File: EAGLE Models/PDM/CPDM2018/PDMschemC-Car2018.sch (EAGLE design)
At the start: 26 parts

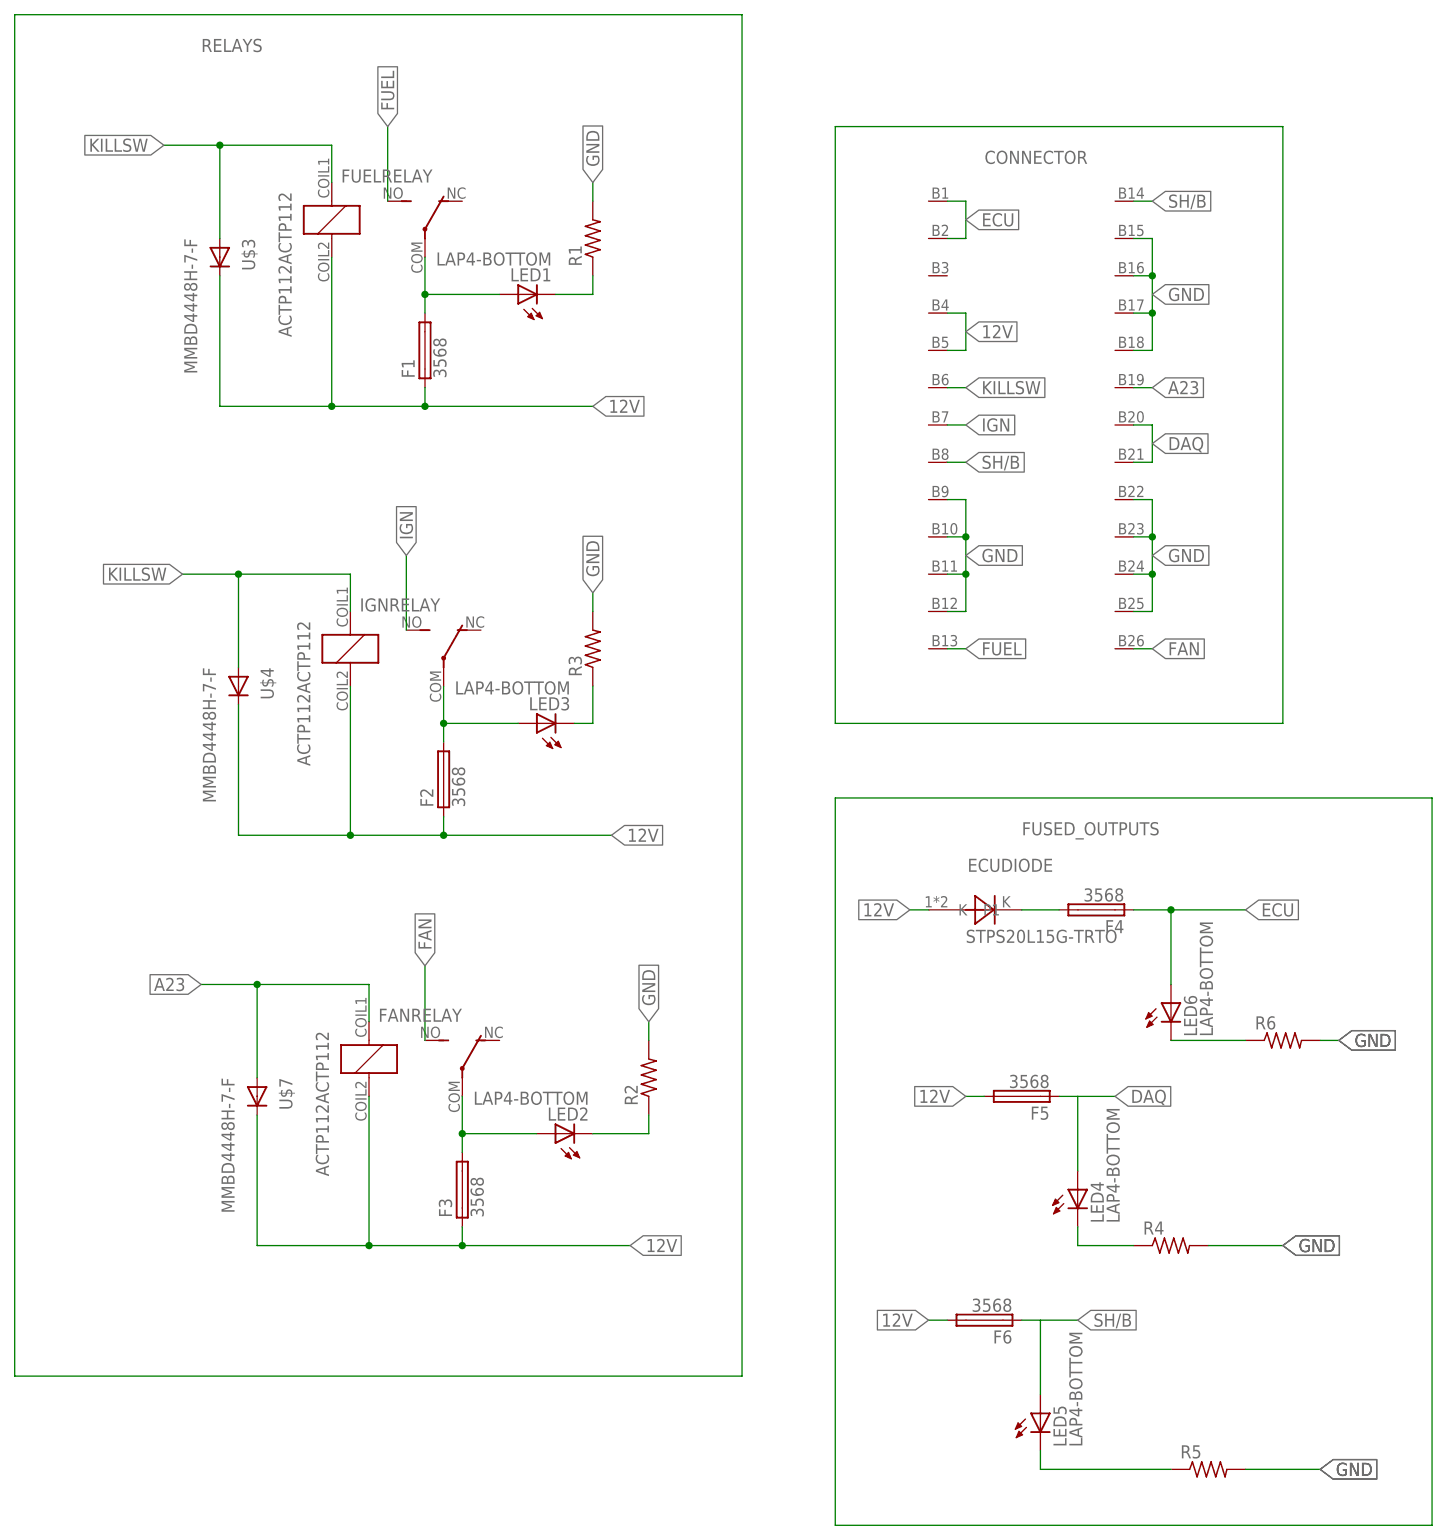
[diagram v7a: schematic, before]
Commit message: Made changes to PDM board
replaced LEDs and Resistors with correct device/package
made ground plane on both layers
named all planes to remove airwires
added resistor values to schem
connected ignition trace to ign relay
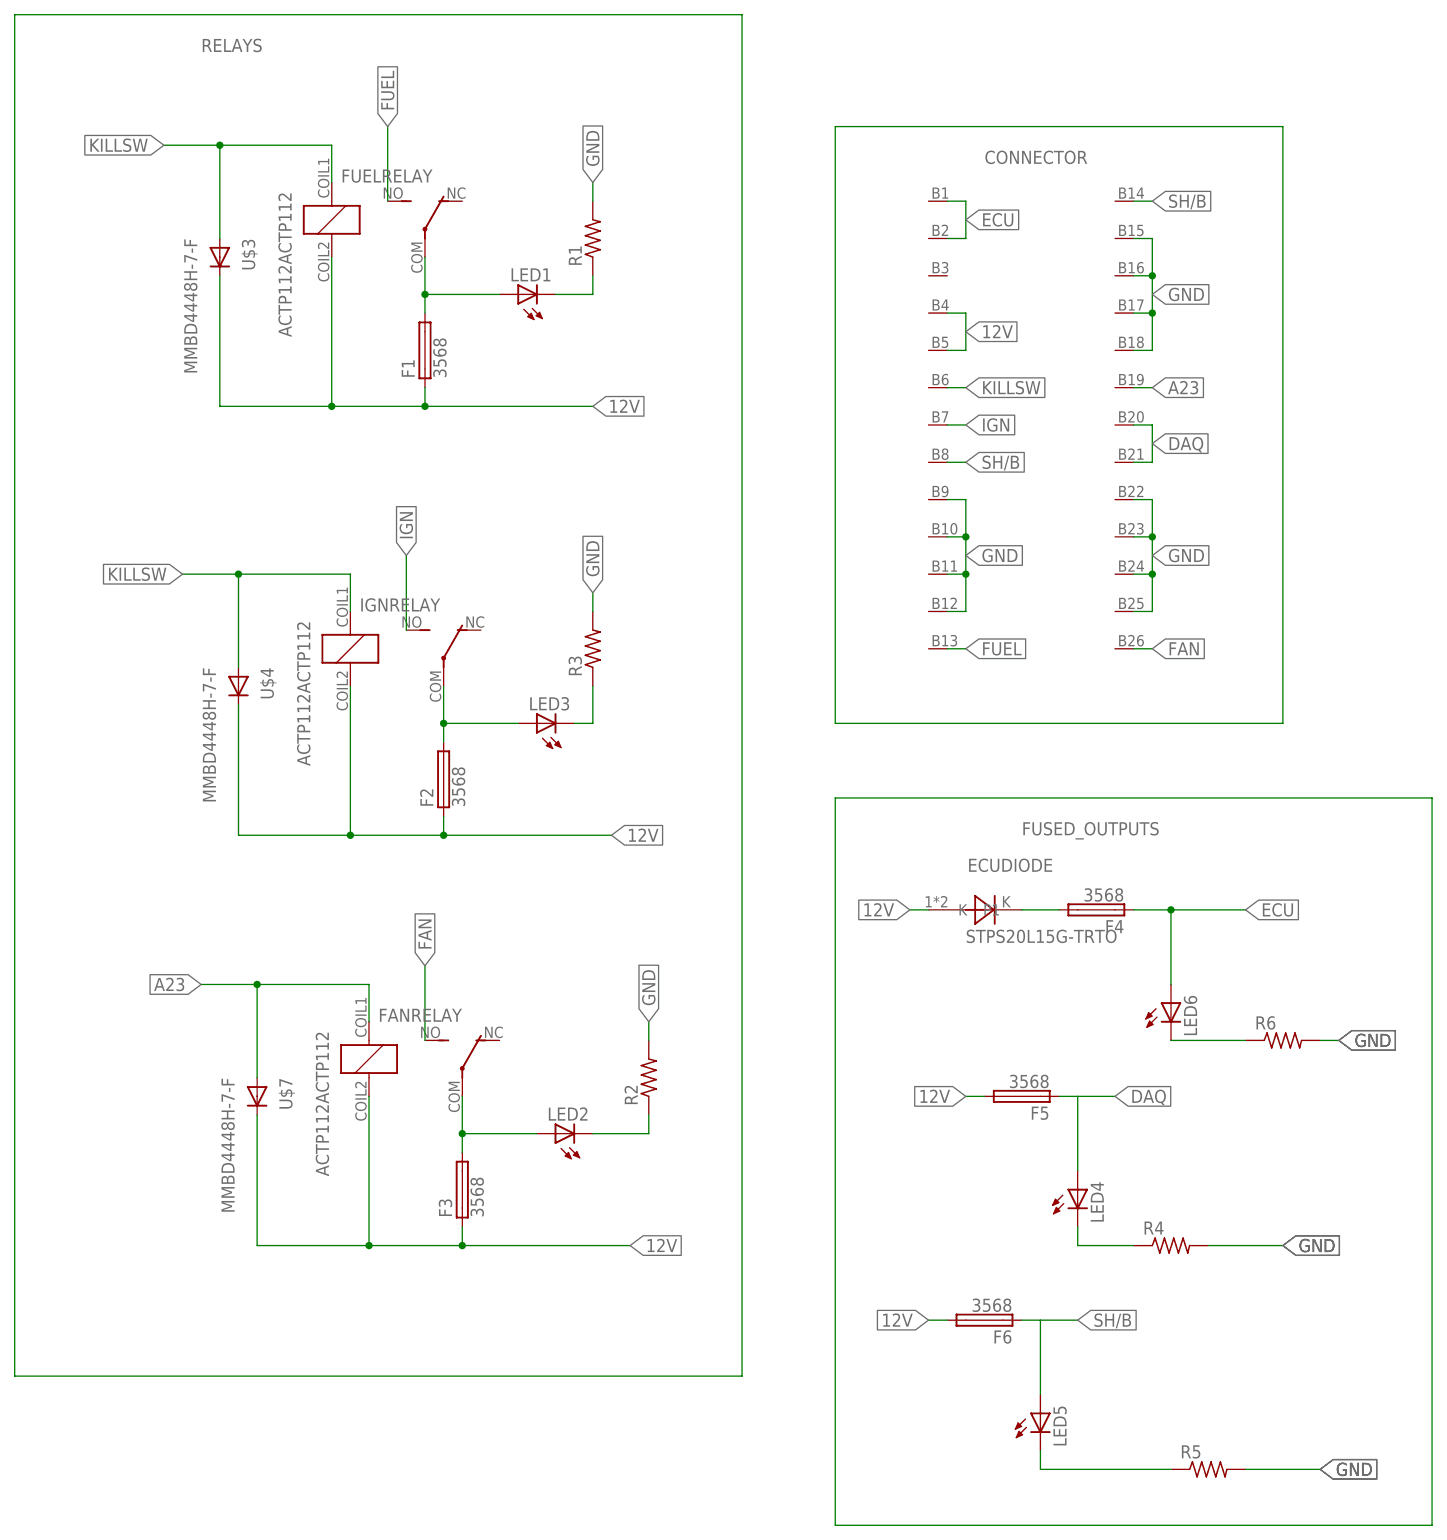
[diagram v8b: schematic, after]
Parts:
- LED1, LED2, LED3, LED4, LED5, LED6: value LAP4-BOTTOM -> (none); device led:LAP4-BOTTOM -> led:LEDCHIPLED_0805
- R1, R2, R3, R4, R5, R6: device resistor:R-US_R1206 -> resistor:R-US_R0805
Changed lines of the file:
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@@
 <part name="U$7" library="diodes-inc" deviceset="MMBD4448H-7-F" device=""/>
 <part name="F3" library="Keystone" deviceset="3568" device=""/>
-<part name="R2" library="resistor" library_urn="urn:adsk.eagle:library:348" deviceset="R-US_" device="R1206" package3d_urn="urn:adsk.eagle:package:26062/1"/>
-<part name="LED2" library="led" library_urn="urn:adsk.eagle:library:259" deviceset="*P4" device="-BOTTOM" package3d_urn="urn:adsk.eagle:package:15878/1" technology="LA"/>
+<part name="R2" library="resistor" library_urn="urn:adsk.eagle:library:348" deviceset="R-US_" device="R0805" package3d_urn="urn:adsk.eagle:package:26059/1"/>
+<part name="LED2" library="led" library_urn="urn:adsk.eagle:library:259" deviceset="LED" device="CHIPLED_0805" package3d_urn="urn:adsk.eagle:package:15821/1"/>
 <part name="F5" library="Keystone" deviceset="3568" device=""/>
 <part name="F4" library="Keystone" deviceset="3568" device=""/>
 <part name="ECUDIODE" library="st-microelectronics" deviceset="STPS20L15G-TR" device="TO"/>
-<part name="R6" library="resistor" library_urn="urn:adsk.eagle:library:348" deviceset="R-US_" device="R1206" package3d_urn="urn:adsk.eagle:package:26062/1"/>
-<part name="LED6" library="led" library_urn="urn:adsk.eagle:library:259" deviceset="*P4" device="-BOTTOM" package3d_urn="urn:adsk.eagle:package:15878/1" technology="LA"/>
+<part name="R6" library="resistor" library_urn="urn:adsk.eagle:library:348" deviceset="R-US_" device="R0805" package3d_urn="urn:adsk.eagle:package:26059/1"/>
+<part name="LED6" library="led" library_urn="urn:adsk.eagle:library:259" deviceset="LED" device="CHIPLED_0805" package3d_urn="urn:adsk.eagle:package:15821/1"/>
 <part name="FUELRELAY" library="panasonic" deviceset="ACTP112" device="ACTP112"/>
 <part name="U$3" library="diodes-inc" deviceset="MMBD4448H-7-F" device=""/>
@@
 <part name="F2" library="Keystone" deviceset="3568" device=""/>
 <part name="F6" library="Keystone" deviceset="3568" device=""/>
-<part name="R4" library="resistor" library_urn="urn:adsk.eagle:library:348" deviceset="R-US_" device="R1206" package3d_urn="urn:adsk.eagle:package:26062/1"/>
-<part name="LED4" library="led" library_urn="urn:adsk.eagle:library:259" deviceset="*P4" device="-BOTTOM" package3d_urn="urn:adsk.eagle:package:15878/1" technology="LA"/>
-<part name="R5" library="resistor" library_urn="urn:adsk.eagle:library:348" deviceset="R-US_" device="R1206" package3d_urn="urn:adsk.eagle:package:26062/1"/>
-<part name="LED5" library="led" library_urn="urn:adsk.eagle:library:259" deviceset="*P4" device="-BOTTOM" package3d_urn="urn:adsk.eagle:package:15878/1" technology="LA"/>
-<part name="R3" library="resistor" library_urn="urn:adsk.eagle:library:348" deviceset="R-US_" device="R1206" package3d_urn="urn:adsk.eagle:package:26062/1"/>
-<part name="LED3" library="led" library_urn="urn:adsk.eagle:library:259" deviceset="*P4" device="-BOTTOM" package3d_urn="urn:adsk.eagle:package:15878/1" technology="LA"/>
-<part name="R1" library="resistor" library_urn="urn:adsk.eagle:library:348" deviceset="R-US_" device="R1206" package3d_urn="urn:adsk.eagle:package:26062/1"/>
-<part name="LED1" library="led" library_urn="urn:adsk.eagle:library:259" deviceset="*P4" device="-BOTTOM" package3d_urn="urn:adsk.eagle:package:15878/1" technology="LA"/>
+<part name="R4" library="resistor" library_urn="urn:adsk.eagle:library:348" deviceset="R-US_" device="R0805" package3d_urn="urn:adsk.eagle:package:26059/1"/>
+<part name="LED4" library="led" library_urn="urn:adsk.eagle:library:259" deviceset="LED" device="CHIPLED_0805" package3d_urn="urn:adsk.eagle:package:15821/1"/>
+<part name="R5" library="resistor" library_urn="urn:adsk.eagle:library:348" deviceset="R-US_" device="R0805" package3d_urn="urn:adsk.eagle:package:26059/1"/>
+<part name="LED5" library="led" library_urn="urn:adsk.eagle:library:259" deviceset="LED" device="CHIPLED_0805" package3d_urn="urn:adsk.eagle:package:15821/1"/>
+<part name="R3" library="resistor" library_urn="urn:adsk.eagle:library:348" deviceset="R-US_" device="R0805" package3d_urn="urn:adsk.eagle:package:26059/1"/>
+<part name="LED3" library="led" library_urn="urn:adsk.eagle:library:259" deviceset="LED" device="CHIPLED_0805" package3d_urn="urn:adsk.eagle:package:15821/1"/>
+<part name="R1" library="resistor" library_urn="urn:adsk.eagle:library:348" deviceset="R-US_" device="R0805" package3d_urn="urn:adsk.eagle:package:26059/1"/>
+<part name="LED1" library="led" library_urn="urn:adsk.eagle:library:259" deviceset="LED" device="CHIPLED_0805" package3d_urn="urn:adsk.eagle:package:15821/1"/>
 </parts>
 <sheets>
